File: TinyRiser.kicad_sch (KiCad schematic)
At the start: 25 parts, among them J2 Bus_PCI_Express_x16, J3 Bus_M.2_Socket_M, J4 fancontrol_header, M1 Fan_4pin

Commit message: starting to add smbus to fan control header
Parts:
- added J5: Conn_02x04_Odd_Even, Connector_PinSocket_2.54mm:PinSocket_2x04_P2.54mm_Horizontal, symbol Connector_Generic:Conn_02x04_Odd_Even
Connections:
- net +12V: now also J5.2 (Pin_2)
- net +12V_fan: now also J5.1 (Pin_1)
- net +3V3: now also J5.4 (Pin_4)
- net GND: now also J5.6 (Pin_6)
- net PWM_fan: now also J5.5 (Pin_5)
- net SMBCLK: now also J5.8 (Pin_8)
- net SMBDATA: now also J5.7 (Pin_7)
- net Taco_fan: now also J5.3 (Pin_3)
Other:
- moved on the sheet: C1, C2, C3, D1, H1, J1, J2, J3, J4, JP1, M1, R1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

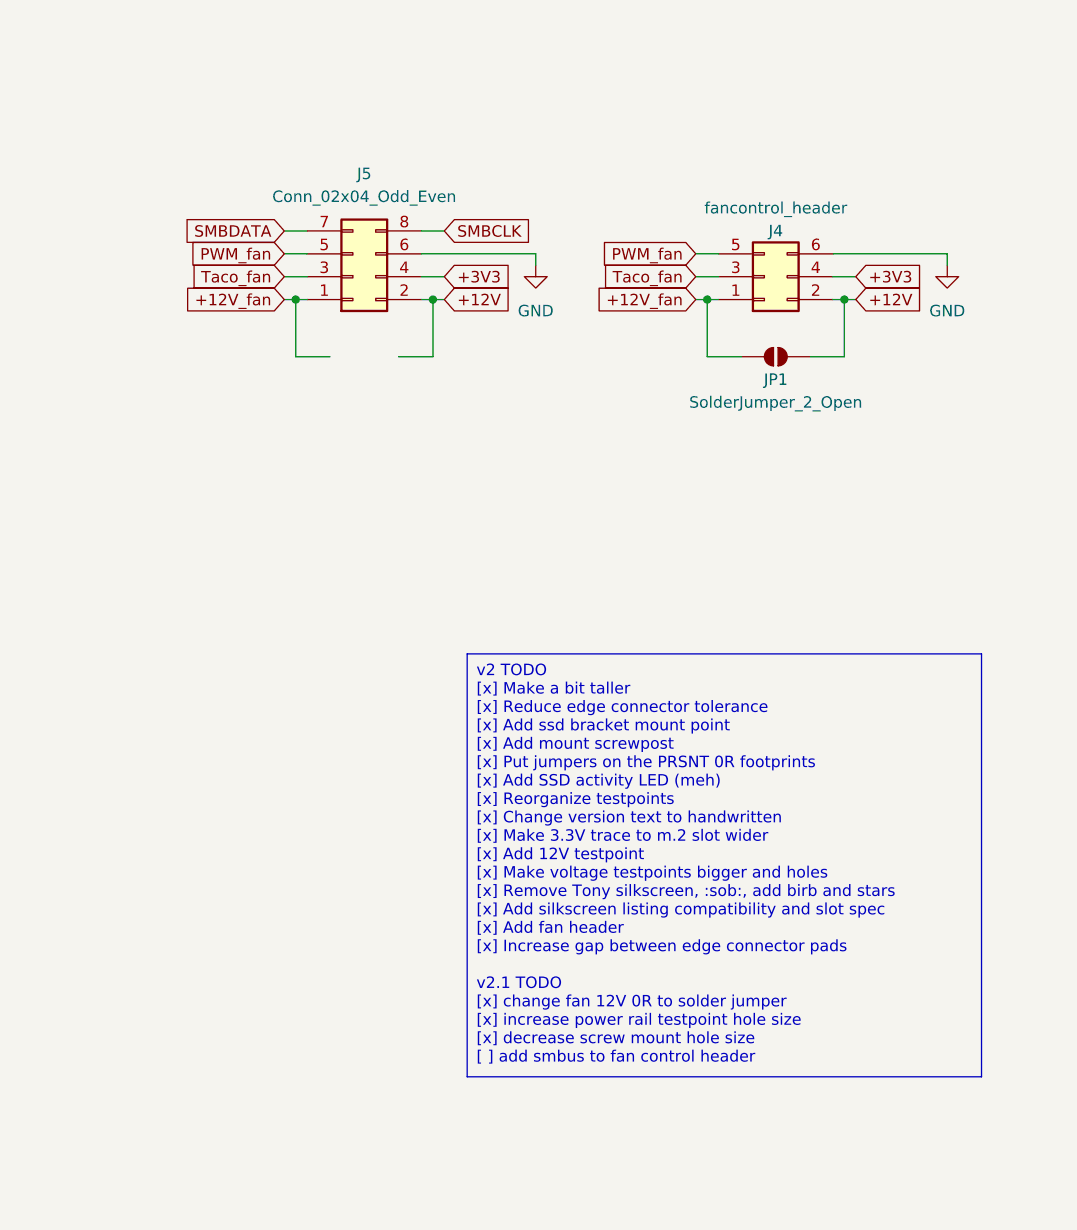
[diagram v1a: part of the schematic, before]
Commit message: Finished adding smbus to fan control header
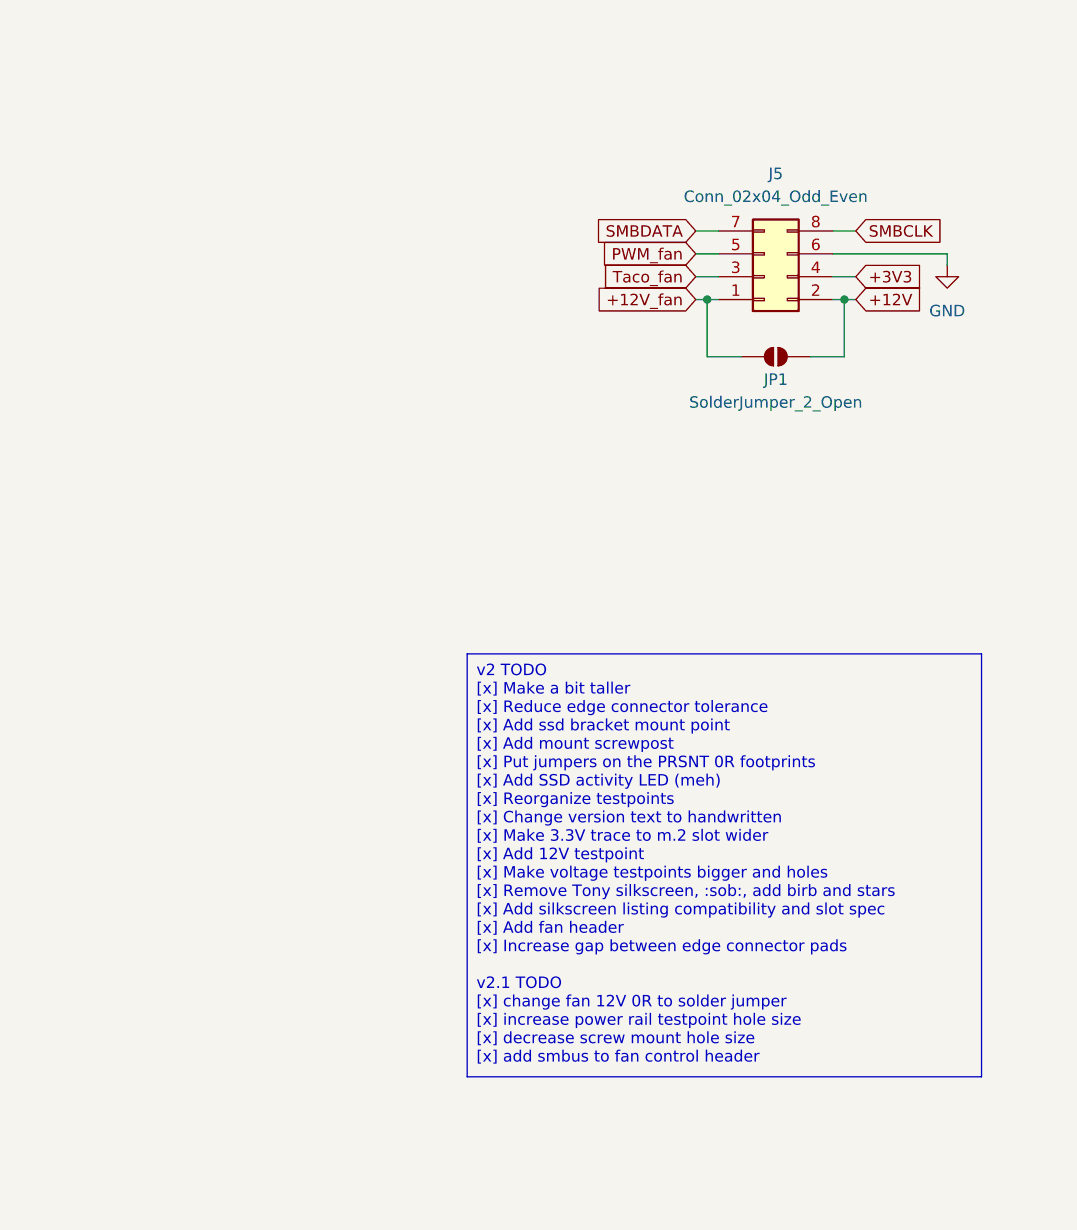
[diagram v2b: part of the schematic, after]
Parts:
- removed J4: fancontrol_header, Connector_PinSocket_2.54mm:PinSocket_2x03_P2.54mm_Horizontal, symbol Connector_Generic:Conn_02x03_Odd_Even
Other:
- moved on the sheet: J5

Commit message: Added some notes
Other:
- note added: "Note: CLKREQ# needs to be connected to GND to activate the clock signal. If you're replacing the PCIe slot with an open-ended one, make sure to account for longer cards where the presence pin is outside the slot. Maybe just hard-wire CLKREQ# to GND"
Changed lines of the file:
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@@
+		)
+	)
+	(text "Note: CLKREQ# needs to be connected to GND to activate the clock signal.\nIf you're replacing the PCIe slot with an open-ended one,\nmake sure to account for longer cards where the presence pin is outside the slot.\nMaybe just hard-wire CLKREQ# to GND"
+		(exclude_from_sim no)
+		(at 237.744 22.606 0)
+		(effects
+			(font
+				(size 1.27 1.27)
+			)
+			(justify left)
 		)
 	)
